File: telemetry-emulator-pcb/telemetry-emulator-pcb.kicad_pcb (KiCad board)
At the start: 2 copper layers, 100 x 50 mm, 47 parts, among them IC1 ATmega328P-A, IC2 MCP2515-xSO, IC3 MCP2551-I-SN, J1 USB_B_Micro, J2 ENABLE_RX, J3 5V-3V3, J4 Conn_02x14_Odd_Even, J5 CAN_TERM, J6 UART, J7 CAN, J8 CAN, J9 CAN, Q1 BSS138, Q2 BSS138, U1 CH340C, Y1 16MHz, Y2 8MHz

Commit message: Minor changes
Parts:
- moved C1 0.50 mm to (130.6, 91.9)
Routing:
- net +5V: track 12.9 -> 15.7 mm
- net Earth: track 84.7 -> 85.5 mm
- net RX_USB: track 92.5 -> 92.6 mm, vias 2 -> 4
- net TX: vias 4 -> 6

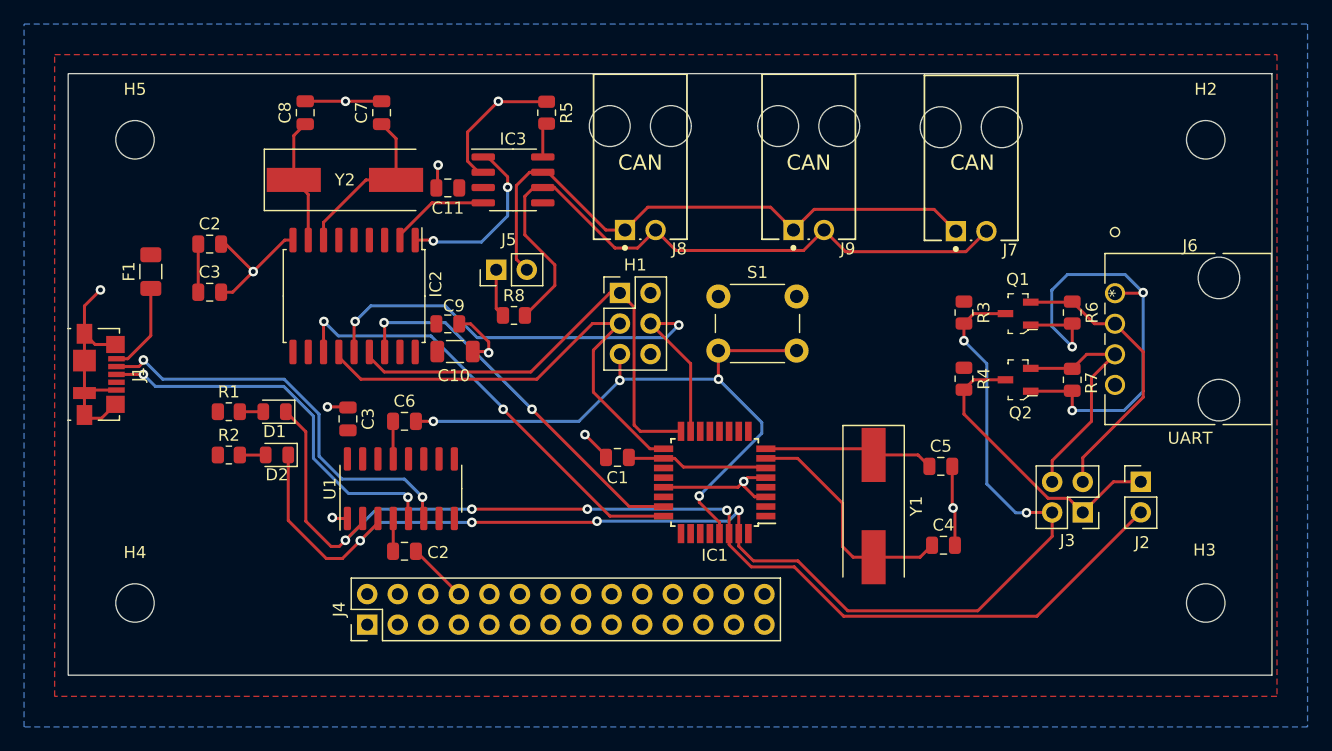
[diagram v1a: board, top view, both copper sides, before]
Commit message: Adds tracks for gpio header
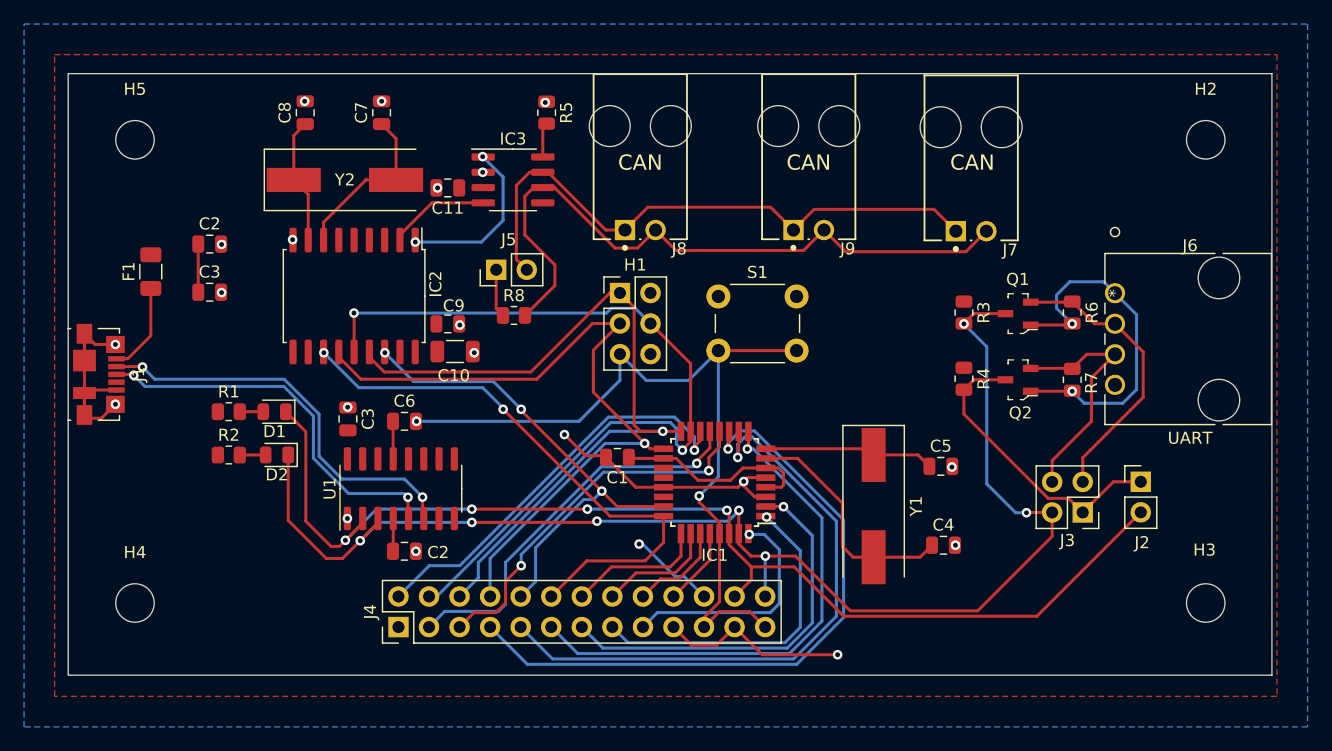
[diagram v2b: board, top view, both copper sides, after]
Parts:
- J4: value Conn_02x14_Odd_Even -> Conn_02x13_Odd_Even; footprint Connector_PinHeader_2.54mm:PinHeader_2x14_P2.54mm_Vertical -> Connector_PinHeader_2.54mm:PinHeader_2x13_P2.54mm_Vertical
- moved J4 2.61 mm to (112.4, 106.0)
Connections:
- IC1 pad 1: unconnected-(IC1-Pad1) -> D3
- IC1 pad 10: unconnected-(IC1-Pad10) -> D6
- IC1 pad 11: unconnected-(IC1-Pad11) -> D7
- IC1 pad 12: unconnected-(IC1-Pad12) -> D8
- IC1 pad 13: unconnected-(IC1-Pad13) -> D9
- IC1 pad 14: unconnected-(IC1-Pad14) -> D10
- IC1 pad 2: unconnected-(IC1-Pad2) -> D4
- IC1 pad 25: unconnected-(IC1-Pad25) -> A2
- IC1 pad 26: unconnected-(IC1-Pad26) -> A3
- IC1 pad 27: unconnected-(IC1-Pad27) -> A4
- IC1 pad 28: unconnected-(IC1-Pad28) -> A5
- IC1 pad 32: unconnected-(IC1-Pad32) -> D2
- IC1 pad 9: unconnected-(IC1-Pad9) -> D5
- J4 pad 1: unconnected-(J4-Pad1) -> Earth
- J4 pad 10: unconnected-(J4-Pad10) -> CAN_CS
- J4 pad 11: unconnected-(J4-Pad11) -> D5
- J4 pad 12: unconnected-(J4-Pad12) -> CAN_INT
- J4 pad 13: unconnected-(J4-Pad13) -> D4
- J4 pad 14: unconnected-(J4-Pad14) -> A2
- J4 pad 15: unconnected-(J4-Pad15) -> D3
- J4 pad 16: unconnected-(J4-Pad16) -> A3
- J4 pad 17: unconnected-(J4-Pad17) -> D2
- J4 pad 18: unconnected-(J4-Pad18) -> A4
- J4 pad 19: unconnected-(J4-Pad19) -> Earth
- J4 pad 2: unconnected-(J4-Pad2) -> D10
- J4 pad 20: unconnected-(J4-Pad20) -> A5
- J4 pad 21: unconnected-(J4-Pad21) -> reset
- J4 pad 22: unconnected-(J4-Pad22) -> +5V
- J4 pad 23: unconnected-(J4-Pad23) -> Earth
- J4 pad 24: unconnected-(J4-Pad24) -> RX_USB
- J4 pad 25: unconnected-(J4-Pad25) -> reset
- J4 pad 26: unconnected-(J4-Pad26) -> TX
- J4 pad 3: unconnected-(J4-Pad3) -> D9
- J4 pad 4: unconnected-(J4-Pad4) -> MOSI
- J4 pad 5: unconnected-(J4-Pad5) -> D8
- J4 pad 6: unconnected-(J4-Pad6) -> MISO
- J4 pad 7: unconnected-(J4-Pad7) -> D7
- J4 pad 8: Earth -> SCK
- J4 pad 9: unconnected-(J4-Pad9) -> D6
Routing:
- net D7: track 0.00 -> 55.5 mm, vias 0 -> 1
- net D6: track 0.00 -> 50.9 mm, vias 0 -> 1
- net D5: track 0.00 -> 43.2 mm, vias 0 -> 1
- net D10: track 0.00 -> 33.6 mm, vias 0 -> 1
- net D9: track 0.00 -> 33.0 mm, vias 0 -> 1
- net D4: track 0.00 -> 32.9 mm, vias 0 -> 1
- net Earth: track 85.5 -> 53.0 mm, vias 11 -> 20
- net D8: track 0.00 -> 31.3 mm, vias 0 -> 2
- net D3: track 0.00 -> 27.1 mm, vias 0 -> 1
- net MOSI: track 44.3 -> 70.1 mm
- net MISO: track 40.1 -> 63.4 mm, vias 0 -> 1
- net SCK: track 40.9 -> 60.8 mm, vias 0 -> 1
- net D2: track 0.00 -> 19.8 mm, vias 0 -> 1
- net reset: track 54.8 -> 68.1 mm, vias 4 -> 2
- net +5V: track 15.7 -> 28.0 mm, vias 0 -> 1
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
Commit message: Small change
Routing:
- net TX: track 111.8 -> 111.7 mm, vias 7 -> 6
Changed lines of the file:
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@@
   (segment (start 128.1 96.2) (end 139.6 96.2) (width 0.25) (layer "B.Cu") (net 27))
   (segment (start 110.576752 96.2) (end 107.988376 98.788376) (width 0.25) (layer "B.Cu") (net 27))
-  (segment (start 164.625 96.475) (end 166.735 96.475) (width 0.25) (layer "F.Cu") (net 28))
   (segment (start 106.4 100.3) (end 107.746751 100.3) (width 0.25) (layer "F.Cu") (net 28))
   (segment (start 140.684 98.23) (end 140.684 96.315503) (width 0.25) (layer "F.Cu") (net 28))
@@
   (segment (start 142.9 100.1) (end 141.7 100.1) (width 0.25) (layer "F.Cu") (net 28))
   (segment (start 162.852 79.947) (end 160.227 79.947) (width 0.25) (layer "F.Cu") (net 28))
-  (segment (start 164.6 96.5) (end 164.625 96.475) (width 0.25) (layer "F.Cu") (net 28))
   (segment (start 107.746751 100.3) (end 109.223375 98.823375) (width 0.25) (layer "F.Cu") (net 28))
-  (via blind (at 164.6 96.5) (size 0.8) (drill 0.4) (layers "F.Cu" "B.Cu") (free) (net 28))
   (via (at 128.9 97.2) (size 0.8) (drill 0.4) (layers "F.Cu" "B.Cu") (net 28))
   (via (at 159.4 80.8) (size 0.8) (drill 0.4) (layers "F.Cu" "B.Cu") (free) (net 28))
@@
   (via (at 140.699503 96.3) (size 0.8) (drill 0.4) (layers "F.Cu" "B.Cu") (net 28))
   (via (at 118.5 97.3) (size 0.8) (drill 0.4) (layers "F.Cu" "B.Cu") (net 28))
-  (segment (start 161.3 94.1) (end 163.7 96.5) (width 0.25) (layer "B.Cu") (net 28))
+  (segment (start 163.675 96.475) (end 166.735 96.475) (width 0.25) (layer "B.Cu") (net 28))
+  (segment (start 161.3 94.1) (end 163.675 96.475) (width 0.25) (layer "B.Cu") (net 28))
   (segment (start 139.825305 97.2) (end 140.699503 96.325802) (width 0.25) (layer "B.Cu") (net 28))
   (segment (start 142.9 100.1) (end 142.88 100.12) (width 0.25) (layer "B.Cu") (net 28))
-  (segment (start 159.4 80.8) (end 161.3 82.7) (width 0.25) (layer "B.Cu") (net 28))
   (segment (start 142.88 100.12) (end 142.88 103.46) (width 0.25) (layer "B.Cu") (net 28))
-  (segment (start 163.7 96.5) (end 164.6 96.5) (width 0.25) (layer "B.Cu") (net 28))
+  (segment (start 161.3 82.7) (end 161.3 94.1) (width 0.25) (layer "B.Cu") (net 28))
   (segment (start 110.74675 97.3) (end 109.223375 98.823375) (width 0.25) (layer "B.Cu") (net 28))
   (segment (start 140.699503 96.325802) (end 140.699503 96.3) (width 0.25) (layer "B.Cu") (net 28))
   (segment (start 118.5 97.3) (end 110.74675 97.3) (width 0.25) (layer "B.Cu") (net 28))
   (segment (start 128.9 97.2) (end 139.825305 97.2) (width 0.25) (layer "B.Cu") (net 28))
-  (segment (start 161.3 82.7) (end 161.3 94.1) (width 0.25) (layer "B.Cu") (net 28))
+  (segment (start 159.4 80.8) (end 161.3 82.7) (width 0.25) (layer "B.Cu") (net 28))
   (segment (start 138.284 98.23) (end 138.284 100.436) (width 0.25) (layer "F.Cu") (net 29))
   (segment (start 138.284 100.436) (end 135.26 103.46) (width 0.25) (layer "F.Cu") (net 29))

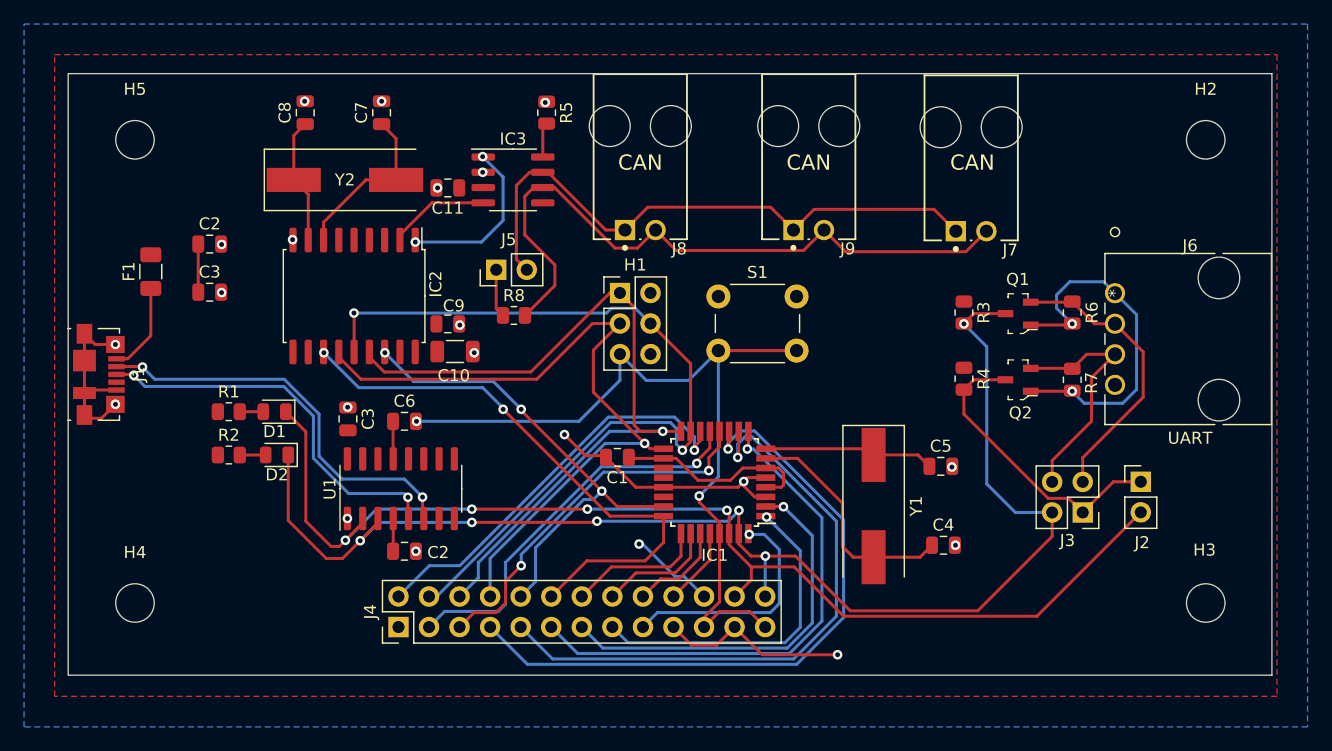
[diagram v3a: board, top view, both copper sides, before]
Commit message: solves potential problem with bypassing logic level shifter
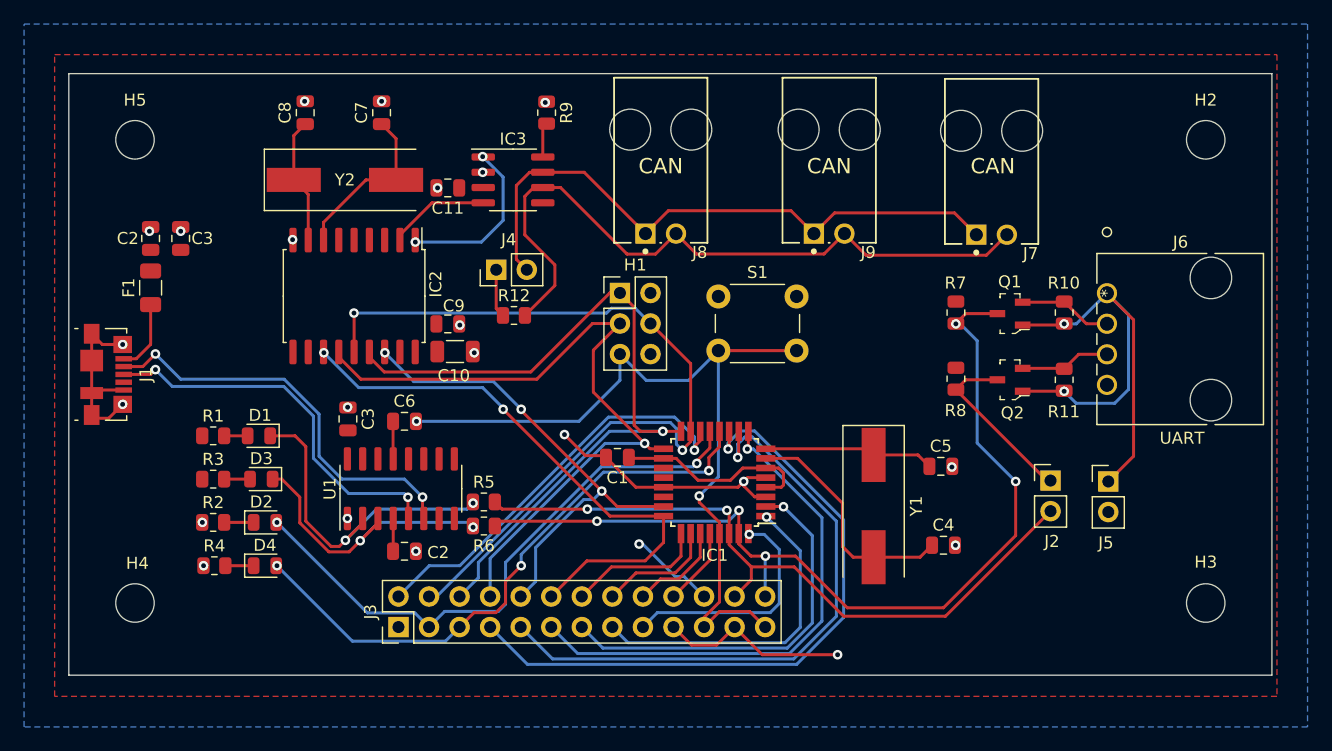
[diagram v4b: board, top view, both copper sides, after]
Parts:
- removed the J3 at (169.3, 96.5)
- added D2: purple, LED_SMD:LED_0805_2012Metric, F.Cu at (101.3, 97.3)
- added D4: blue, LED_SMD:LED_0805_2012Metric, F.Cu at (101.3, 100.9)
- added J5: USE_V_INT, Connector_PinHeader_2.54mm:PinHeader_1x02_P2.54mm_Vertical, F.Cu at (171.4, 93.9)
- added R2: 500, Resistor_SMD:R_0805_2012Metric, F.Cu at (97.0, 97.3)
- added R4: 500, Resistor_SMD:R_0805_2012Metric, F.Cu at (97.1, 100.9)
- added R5: 1K, Resistor_SMD:R_0805_2012Metric, F.Cu at (119.5, 95.6)
- added R6: 1K, Resistor_SMD:R_0805_2012Metric, F.Cu at (119.5, 97.6)
- R1: value 270 -> 1K
- R3: renamed from R2; value 270 -> 1K
- moved J2 7.50 mm to (166.6, 93.8)
- moved C3 5.08 mm to (94.3, 73.7), turned to 90 degrees
- moved C2 4.93 mm to (91.8, 73.7), turned to 90 degrees
- moved D1 2.39 mm to (100.8, 90.1)
- moved D3 2.39 mm to (101.0, 93.7)
- moved R1 2.39 mm to (97.0, 90.1)
- moved R3 2.39 mm to (97.0, 93.7)
- moved J7 1.73 mm to (161.7, 67.3)
- moved J8 1.73 mm to (134.2, 67.2)
- moved J9 1.73 mm to (148.2, 67.2)
- moved F1 1.35 mm to (91.8, 77.8)
- moved J6 0.67 mm to (171.3, 78.2)
- moved Q1 0.67 mm to (163.2, 79.9)
- moved Q2 0.67 mm to (163.2, 85.4)
- moved R10 0.67 mm to (167.7, 79.9)
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- renumbered D2 to D3, J4 to J3, J5 to J4, R6 to R10, R7 to R11, R8 to R12, R3 to R7, R4 to R8, R5 to R9
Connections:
- net 3V3 renamed V_EXT
- D1 pad 1: RX_USB -> Net-(D1-Pad1)
- D3 pad 1: TX -> Net-(D3-Pad1)
- U1 pad 2: RX_USB -> Net-(D1-Pad1)
- U1 pad 3: TX -> Net-(D3-Pad1)
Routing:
- net RX_USB: track 95.6 -> 58.3 mm, vias 4 -> 2
- net TX: track 111.7 -> 78.4 mm, vias 6 -> 5
- net Net-(D1-Pad1): track 0.00 -> 28.2 mm, vias 0 -> 2
- net Net-(D3-Pad1): track 0.00 -> 24.1 mm, vias 0 -> 2
- net D8: track 31.3 -> 49.6 mm, vias 2 -> 3
- net D9: track 33.0 -> 49.3 mm, vias 1 -> 2
- net TX_EXT: track 24.0 -> 7.79 mm
- net V_EXT: track 30.7 -> 44.1 mm
- net RX_EXT: track 20.3 -> 7.52 mm
- net RX: track 25.0 -> 14.8 mm
- net +5V: track 28.0 -> 24.0 mm
- net Net-(D2-Pad1): track 0.00 -> 2.45 mm
- net Net-(D4-Pad1): track 0.00 -> 2.35 mm
- net CANL: track 56.2 -> 58.2 mm
- net CANH: track 49.4 -> 51.2 mm
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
